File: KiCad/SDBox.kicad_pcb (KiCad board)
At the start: 2 copper layers, 47 x 50 mm, 22 parts, among them J1 DB25_Male, J2 USB_B_Micro, J3 Micro_SD_Card_Socket, U1 Arduino_Nano_V3, U2 74LVC3G17, U3 74LVC1G17

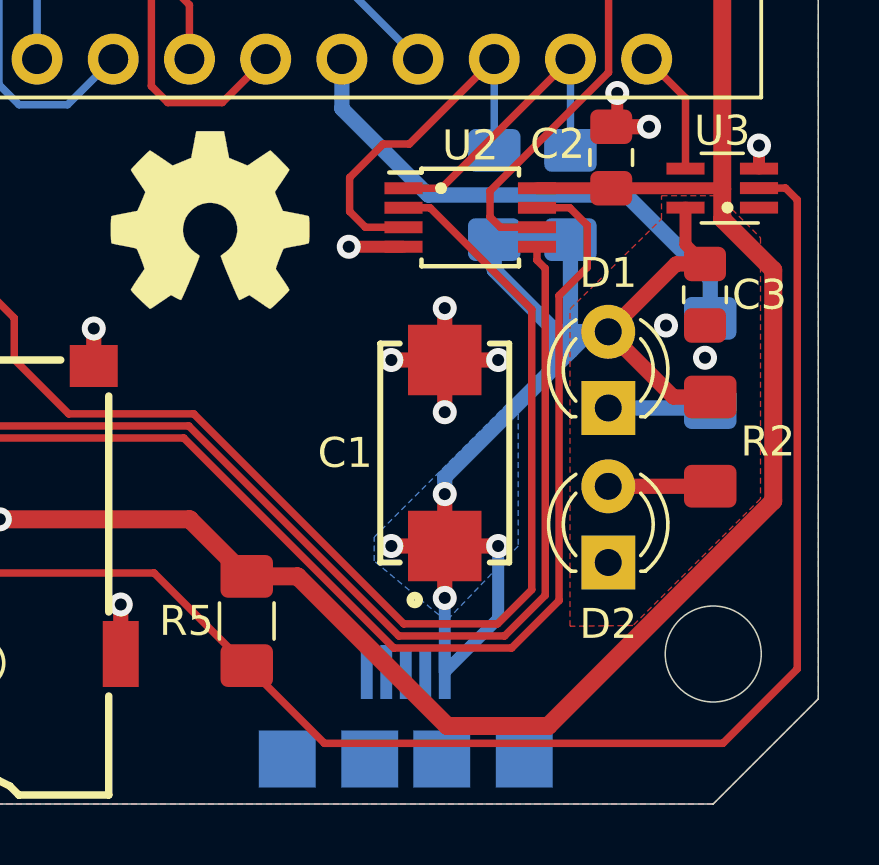
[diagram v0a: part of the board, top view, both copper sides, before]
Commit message: small improvement 3V3-routing
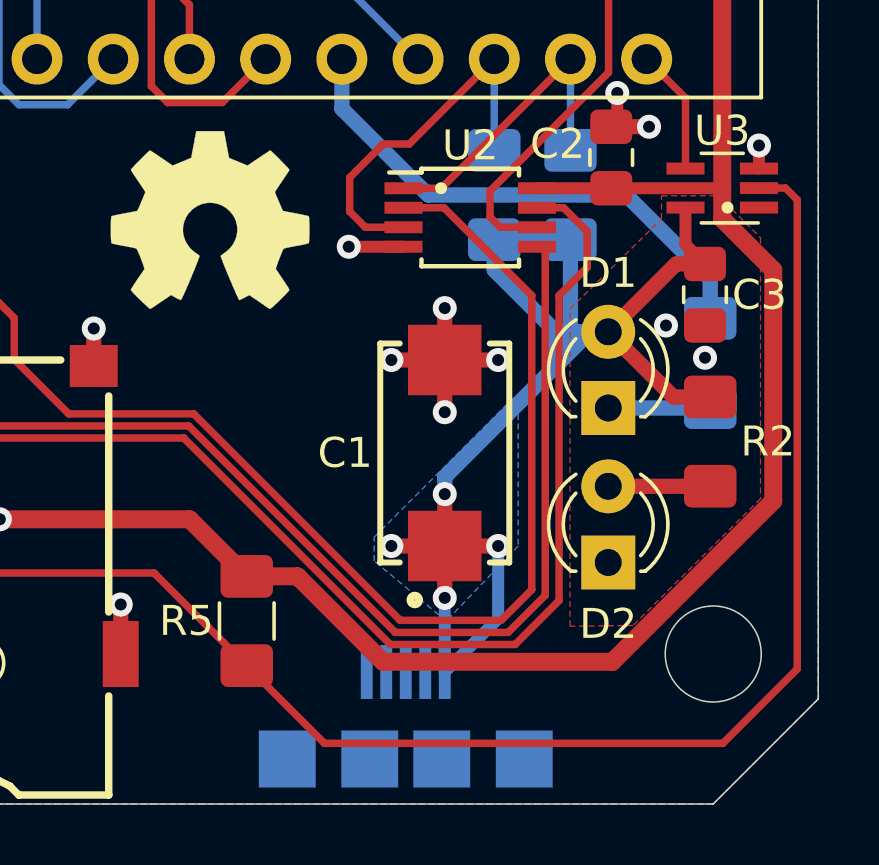
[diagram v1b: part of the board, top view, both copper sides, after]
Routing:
- net 3V3: track 86.5 -> 84.8 mm
